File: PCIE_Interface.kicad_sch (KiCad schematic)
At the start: 1 part, among them J5 MDT275M02001

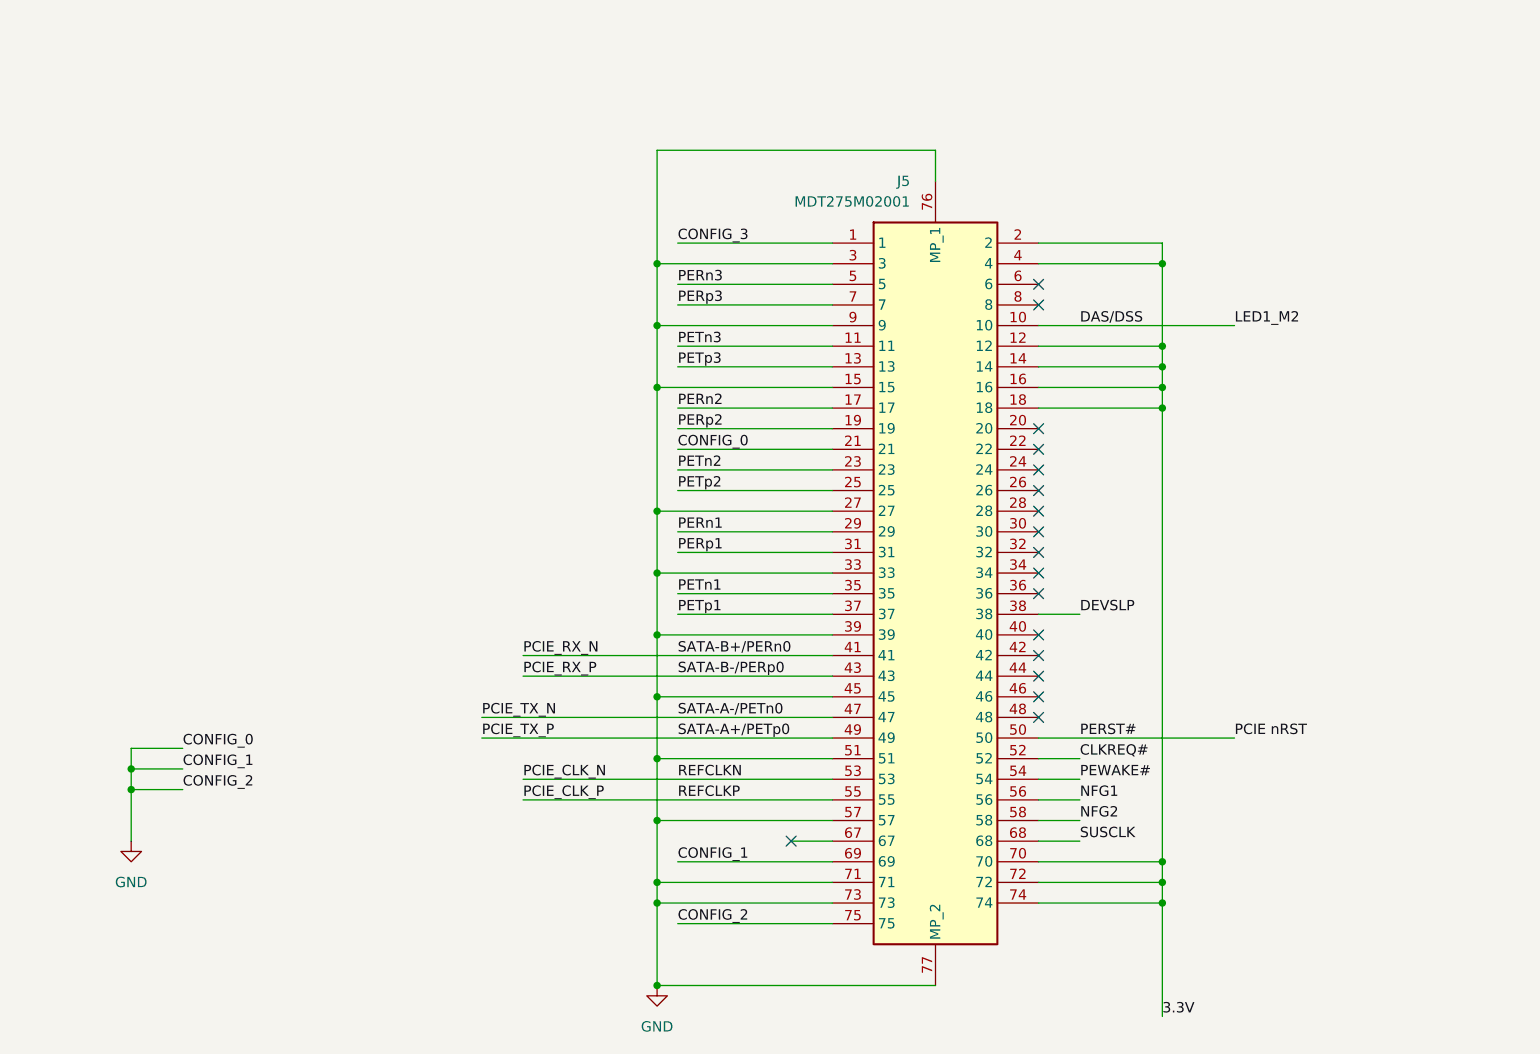
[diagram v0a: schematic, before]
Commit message: multiple changes. fixed some mistakes, added jumper pins for wifi
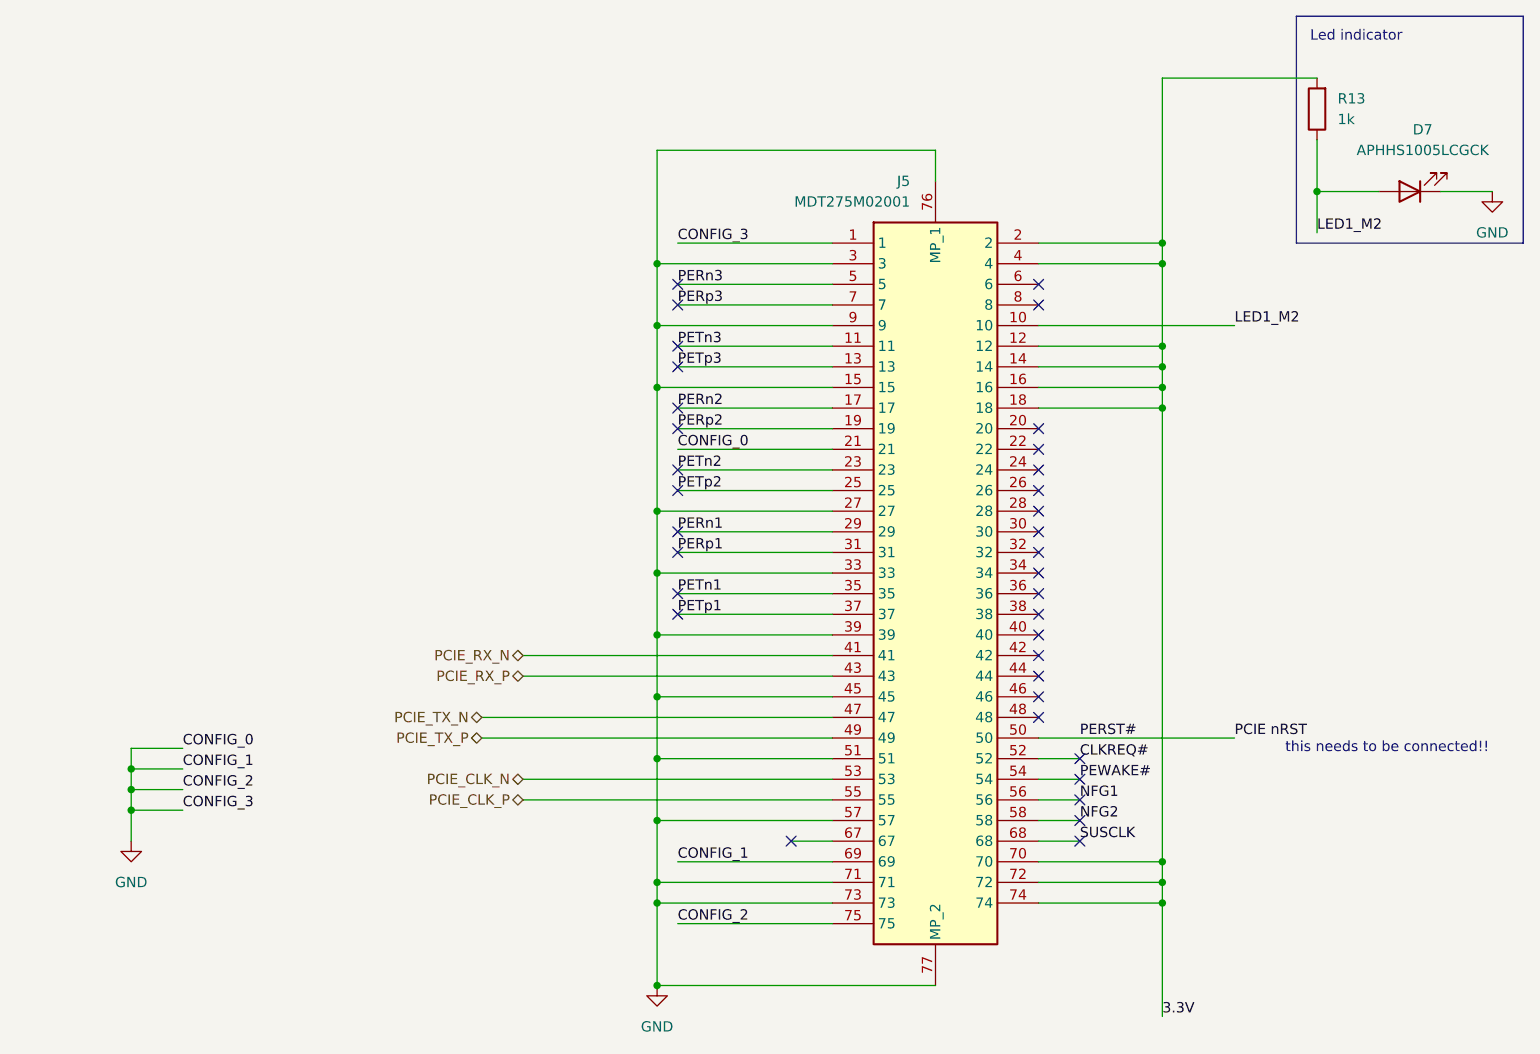
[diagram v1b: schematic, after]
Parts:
- added D7: APHHS1005LCGCK, LED_SMD:LED_0402_1005Metric, symbol #dzdb:s_dio/D-KIN-APHHS1005LCGCK
- added R13: 1k, Resistor_SMD:R_0603_1608Metric, symbol #dzdb:g_res/R-1k-0603
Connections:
- net CONFIG_3 is gone; now on net GND: J5.1
- net 3.3V: now also R13.2
- net GND: now also D7.1 (K)
- net DAS/DSS renamed LED1_M2
- net LED1_M2: now also D7.2 (A), R13.1
- net DEVSLP: no longer names the net of J5.38
- no-connect marks 17 -> 35
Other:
- note added: "Led indicator"
- note added: "this needs to be connected!!"

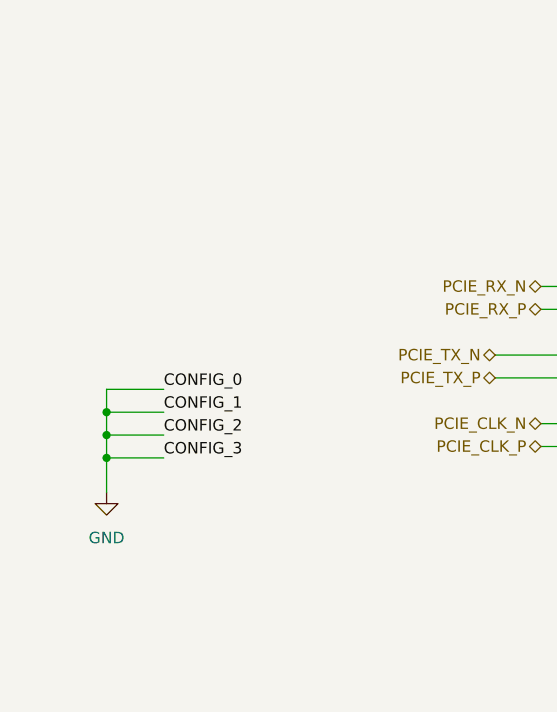
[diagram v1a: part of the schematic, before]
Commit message: connector changes
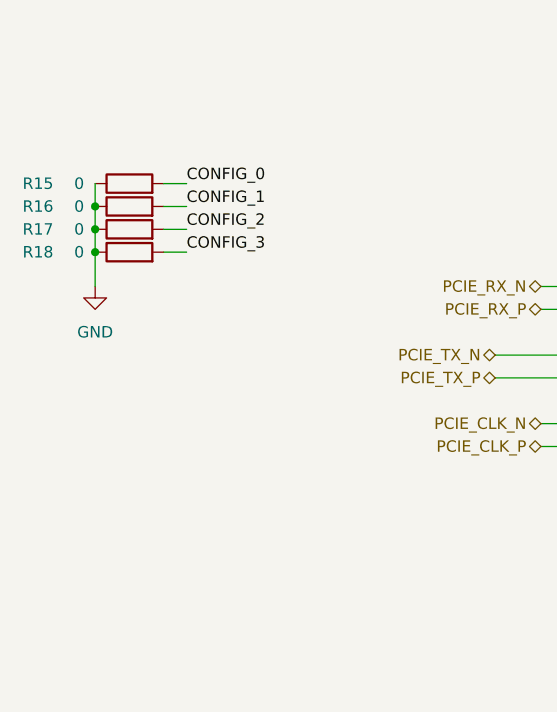
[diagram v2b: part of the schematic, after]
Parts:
- added R15, R16, R17, R18: 0, Resistor_SMD:R_0603_1608Metric, symbol #dzdb:g_res/R-0-0603
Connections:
- net GND: now also R15.1, R16.1, R17.1, R18.1; no longer J5.1, J5.21, J5.69, J5.75
- new net CONFIG_0: J5.21, R15.2
- new net CONFIG_1: J5.69, R16.2
- new net CONFIG_2: J5.75, R17.2
- new net CONFIG_3: J5.1, R18.2

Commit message: added comment boxes
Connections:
- net PCIE nRST renamed PCIE_nRST
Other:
- note removed: "this needs to be connected!!"
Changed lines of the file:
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@@
 		)
 	)
-	(text "this needs to be connected!!\n"
-		(exclude_from_sim no)
-		(at 186.436 140.97 0)
-		(effects
-			(font
-				(size 1.27 1.27)
-			)
-		)
-	)
 	(junction
 		(at 96.52 157.48)
@@
 		)
 	)
-	(label "PCIE nRST"
-		(at 167.64 139.7 0)
-		(effects
-			(font
-				(size 1.27 1.27)
-			)
-			(justify left bottom)
-		)
-	)
 	(label "PERp1"
 		(at 99.06 116.84 0)
@@
 		)
 	)
+	(hierarchical_label "PCIE_nRST"
+		(shape input)
+		(at 167.64 139.7 0)
+		(effects
+			(font
+				(size 1.27 1.27)
+			)
+			(justify left)
+		)
+	)

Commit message: Added Power logic finally. (plus some comments on further improvements)
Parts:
- renumbered R15 to CONFIG_1, R16 to CONFIG_2, R17 to CONFIG_3, R18 to CONFIG_4, D7 to D8, J5 to J6
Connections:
- net 3.3V renamed SSD_IN_3.3V
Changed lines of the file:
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@@
-		)
-	)
-	(label "3.3V"
-		(at 158.75 173.99 0)
-		(effects
-			(font
-				(size 1.27 1.27)
-			)
-			(justify left bottom)
 		)
 	)
@@
 			)
 			(justify left bottom)
+		)
+	)
+	(global_label "SSD_IN_3.3V"
+		(shape input)
+		(at 158.75 173.99 180)
+		(fields_autoplaced yes)
+		(effects
+			(font
+				(size 1.27 1.27)
+			)
+			(justify right)
+		)
+		(property "Intersheetrefs" "${INTERSHEET_REFS}"
+			(at 144.0929 173.99 0)
+			(effects
+				(font
+					(size 1.27 1.27)
+				)
+				(justify right)
+				(hide yes)
+			)
 		)
 	)
@@
 		(on_board yes)
 		(dnp no)
-		(property "Reference" "R16"
-			(at 24.13 120.65 90)
+		(property "Reference" "CONFIG_2"
+			(at 23.114 120.65 90)
 			(effects
 				(font
@@
 			(project "nautilus_mainboard"
 				(path "/ce1819b2-f280-40ed-834f-6fe4d12f809d/c2b6dac3-d6fd-4d5d-bd17-0cff91db88eb/f7f72d9d-a73c-4da1-b97a-073a2603b35d"
-					(reference "R16")
+					(reference "CONFIG_2")
 					(unit 1)
 				)
@@
 		(on_board yes)
 		(dnp no)
-		(property "Reference" "R15"
-			(at 24.13 118.11 90)
+		(property "Reference" "CONFIG_1"
+			(at 23.114 118.11 90)
 			(effects
 				(font
@@
 			(project ""
 				(path "/ce1819b2-f280-40ed-834f-6fe4d12f809d/c2b6dac3-d6fd-4d5d-bd17-0cff91db88eb/f7f72d9d-a73c-4da1-b97a-073a2603b35d"
-					(reference "R15")
+					(reference "CONFIG_1")
 					(unit 1)
 				)
@@
 		(dnp no)
 		(fields_autoplaced yes)
-		(property "Reference" "D7"
+		(property "Reference" "D8"
 			(at 190.8175 64.77 0)
 			(effects
@@
 			(project ""
 				(path "/ce1819b2-f280-40ed-834f-6fe4d12f809d/c2b6dac3-d6fd-4d5d-bd17-0cff91db88eb/f7f72d9d-a73c-4da1-b97a-073a2603b35d"
-					(reference "D7")
+					(reference "D8")
 					(unit 1)
 				)
@@
 		(dnp no)
 		(fields_autoplaced yes)
-		(property "Reference" "#PWR031"
+		(property "Reference" "#PWR026"
 			(at 30.48 135.89 0)
 			(effects
@@
 			(project ""
 				(path "/ce1819b2-f280-40ed-834f-6fe4d12f809d/c2b6dac3-d6fd-4d5d-bd17-0cff91db88eb/f7f72d9d-a73c-4da1-b97a-073a2603b35d"
-					(reference "#PWR031")
+					(reference "#PWR026")
 					(unit 1)
 				)
@@
 		(on_board yes)
 		(dnp no)
-		(property "Reference" "R17"
-			(at 24.13 123.19 90)
+		(property "Reference" "CONFIG_3"
+			(at 23.114 123.19 90)
 			(effects
 				(font
@@
 			(project "nautilus_mainboard"
 				(path "/ce1819b2-f280-40ed-834f-6fe4d12f809d/c2b6dac3-d6fd-4d5d-bd17-0cff91db88eb/f7f72d9d-a73c-4da1-b97a-073a2603b35d"
-					(reference "R17")
+					(reference "CONFIG_3")
 					(unit 1)
 				)
@@
 		(on_board yes)
 		(dnp no)
-		(property "Reference" "R18"
-			(at 24.13 125.73 90)
+		(property "Reference" "CONFIG_4"
+			(at 23.114 125.73 90)
 			(effects
 				(font
@@
 			(project "nautilus_mainboard"
 				(path "/ce1819b2-f280-40ed-834f-6fe4d12f809d/c2b6dac3-d6fd-4d5d-bd17-0cff91db88eb/f7f72d9d-a73c-4da1-b97a-073a2603b35d"
-					(reference "R18")
+					(reference "CONFIG_4")
 					(unit 1)
 				)
@@
 		(on_board yes)
 		(dnp no)
-		(property "Reference" "J5"
+		(property "Reference" "J6"
 			(at 127.6919 71.12 90)
 			(effects
@@
 			(project "nautilus_mainboard"
 				(path "/ce1819b2-f280-40ed-834f-6fe4d12f809d/c2b6dac3-d6fd-4d5d-bd17-0cff91db88eb/f7f72d9d-a73c-4da1-b97a-073a2603b35d"
-					(reference "J5")
+					(reference "J6")
 					(unit 1)
 				)
@@
 		(dnp no)
 		(fields_autoplaced yes)
-		(property "Reference" "#PWR032"
+		(property "Reference" "#PWR028"
 			(at 199.39 78.74 0)
 			(effects
@@
 			(project ""
 				(path "/ce1819b2-f280-40ed-834f-6fe4d12f809d/c2b6dac3-d6fd-4d5d-bd17-0cff91db88eb/f7f72d9d-a73c-4da1-b97a-073a2603b35d"
-					(reference "#PWR032")
+					(reference "#PWR028")
 					(unit 1)
 				)
@@
 		(dnp no)
 		(fields_autoplaced yes)
-		(property "Reference" "#PWR030"
+		(property "Reference" "#PWR027"
 			(at 96.52 176.53 0)
 			(effects
@@
 			(project ""
 				(path "/ce1819b2-f280-40ed-834f-6fe4d12f809d/c2b6dac3-d6fd-4d5d-bd17-0cff91db88eb/f7f72d9d-a73c-4da1-b97a-073a2603b35d"
-					(reference "#PWR030")
+					(reference "#PWR027")
 					(unit 1)
 				)

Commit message: multiple chainges on PCB
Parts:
- J6: Order (none) -> Ordered=True
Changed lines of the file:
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@@
+			)
+		)
+		(property "Order" "Ordered=True"
+			(at 130.81 71.12 90)
+			(effects
+				(font
+					(size 1.27 1.27)
+				)
+				(hide yes)
 			)
 		)

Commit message: chore: multiple cosmetic wiring changes
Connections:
- net SSD_IN_3.3V renamed Battery_Out_3.3V
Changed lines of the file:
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@@
 		)
 	)
-	(global_label "SSD_IN_3.3V"
+	(global_label "Battery_Out_3.3V"
 		(shape input)
 		(at 158.75 173.99 180)
@@
 		)
 		(property "Intersheetrefs" "${INTERSHEET_REFS}"
-			(at 144.0929 173.99 0)
+			(at 139.7992 173.99 0)
 			(effects
 				(font
